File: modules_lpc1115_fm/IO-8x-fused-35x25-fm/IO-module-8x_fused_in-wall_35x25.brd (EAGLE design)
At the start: 35 x 25 mm, 82 parts, among them IC1 LPC1115, IC2 ATAES132A-SHEQ-T, Q2 ASFL, U1 EEPROM, X3 MICROMATCH-10

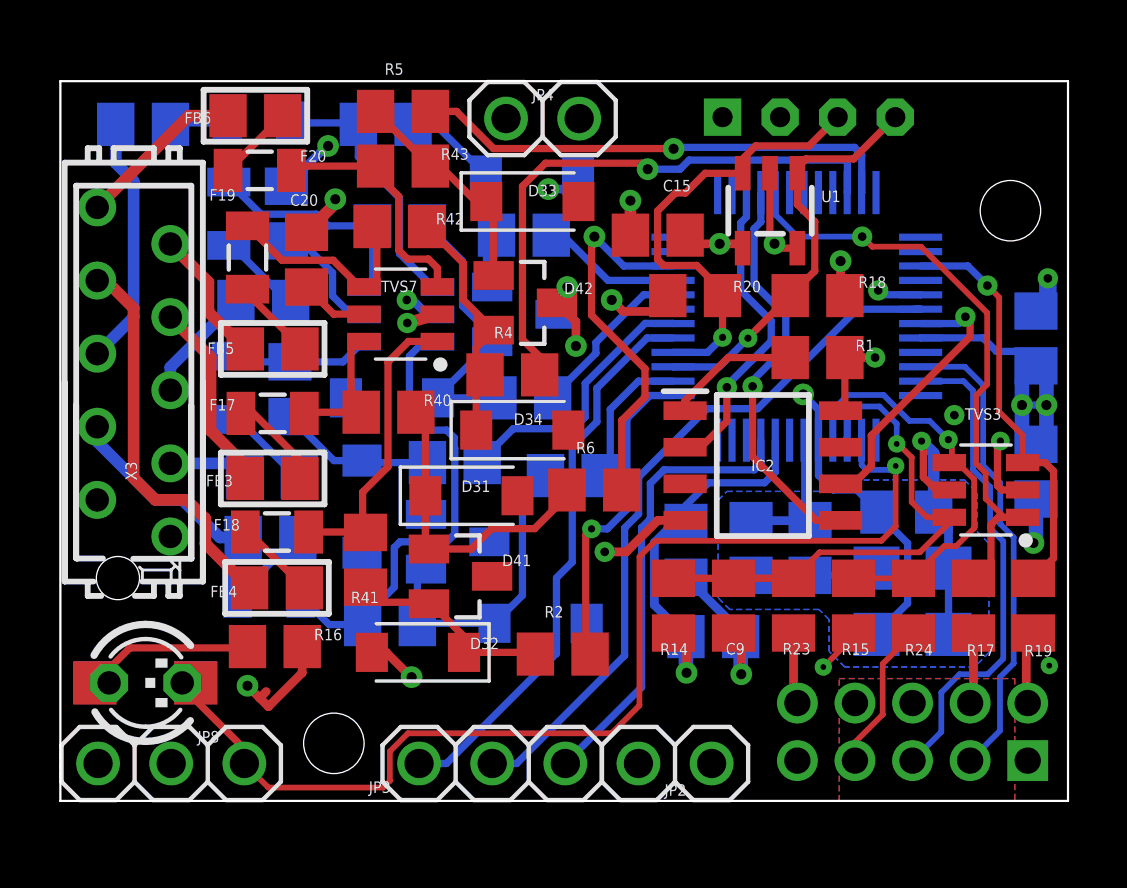
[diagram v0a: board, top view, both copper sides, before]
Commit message: [IOmodule8xUP] added values of 100R resistors; optimized routing
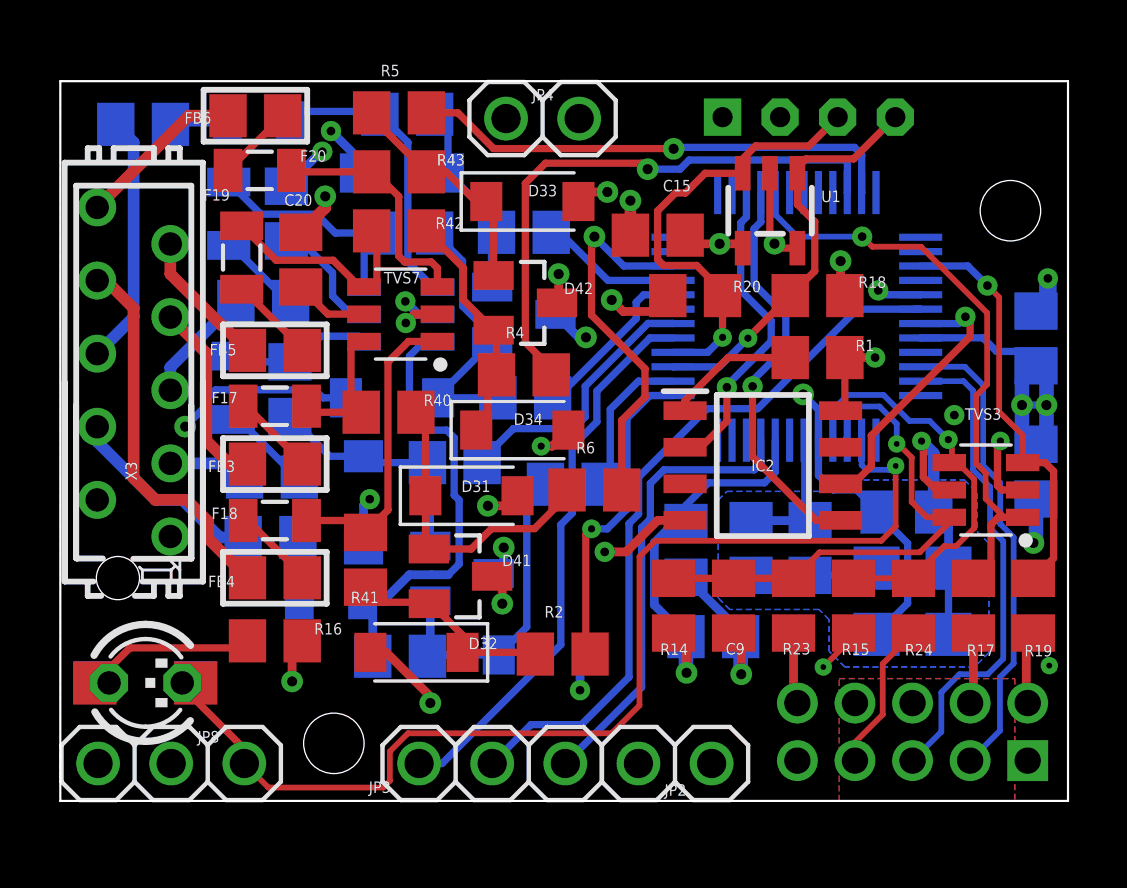
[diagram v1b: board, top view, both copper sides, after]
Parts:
- R2, R3, R4, R5, R6, R7, R8, R9: value 1k -> 100R
- moved D36 4.52 mm to (11.9, 21.8), turned to 0 degrees
- moved F22 2.15 mm to (9.40, 7.06)
- moved R45 1.15 mm to (11.8, 5.03)
- moved D38 1.11 mm to (16.8, 5.07)
- moved D40 1.11 mm to (13.9, 7.90)
- moved R47 0.83 mm to (12.1, 23.9)
- moved FB3 0.51 mm to (7.45, 11.7)
- moved F18 0.41 mm to (7.45, 9.74)
- moved R4 0.40 mm to (16.1, 14.8)
- moved FB4 0.36 mm to (7.45, 7.75)
- moved R46 0.35 mm to (12.1, 19.7)
- moved R3 0.30 mm to (17.8, 11.0)
- moved F17 0.26 mm to (7.45, 13.7)
- moved R43 0.24 mm to (11.8, 21.9)
- moved C20 0.20 mm to (8.35, 18.8)
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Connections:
- net IO1B renamed IO1R
- net IO2B renamed IO2R
- net IO3B renamed IO3R
- net IO4B renamed IO4R
- net IO5B renamed IO5R
- net IO6B renamed IO6R
- net IO7B renamed IO7R
- net IO8B renamed IO8R
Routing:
- net GND: track 40.2 -> 54.9 mm, vias 17 -> 23
- net N$9: track 16.8 -> 15.6 mm
- net IO1R: track 7.26 -> 8.38 mm
- net N$16: track 9.27 -> 10.2 mm
- net N$8: track 3.03 -> 2.11 mm
- net IO7R: track 9.14 -> 8.22 mm
- net +3V3: track 51.6 -> 50.9 mm, vias 12 -> 14
- net N$4: track 3.54 -> 2.97 mm
- net BUS_V: track 25.0 -> 25.5 mm

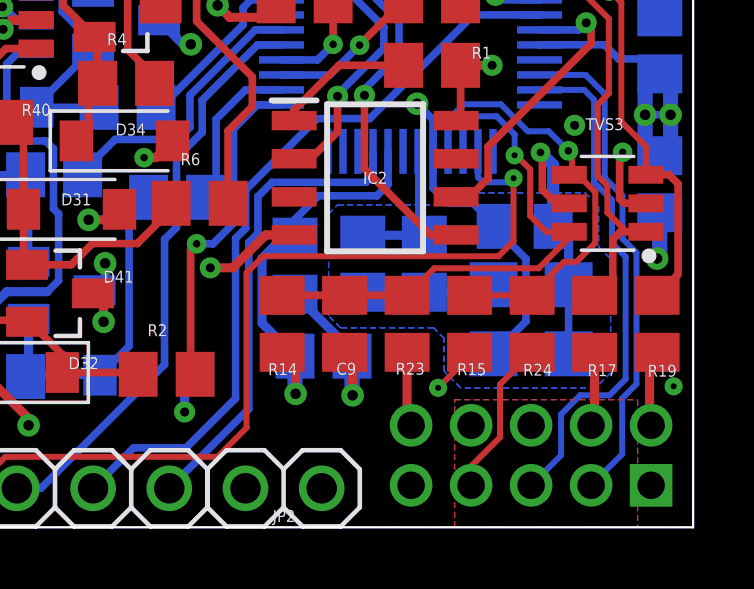
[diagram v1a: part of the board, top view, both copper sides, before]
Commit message: [IOmodule8xUP] moved ISP parts closer to PCB edge
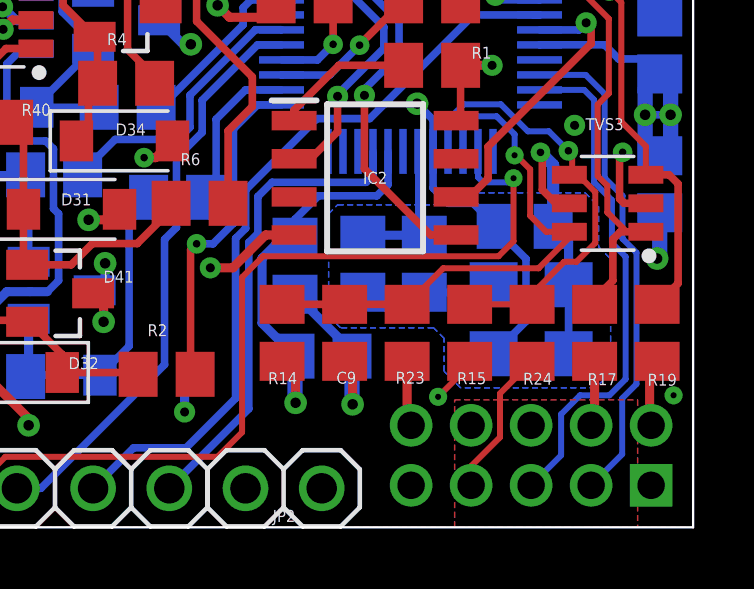
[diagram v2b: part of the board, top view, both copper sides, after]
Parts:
- moved C9 0.30 mm to (23.4, 6.48)
- moved R14 0.30 mm to (21.3, 6.48)
- moved R15 0.30 mm to (27.5, 6.48)
- moved R17 0.30 mm to (31.7, 6.48)
- moved R19 0.30 mm to (33.8, 6.48)
- moved R23 0.30 mm to (25.5, 6.48)
- moved R24 0.30 mm to (29.6, 6.48)

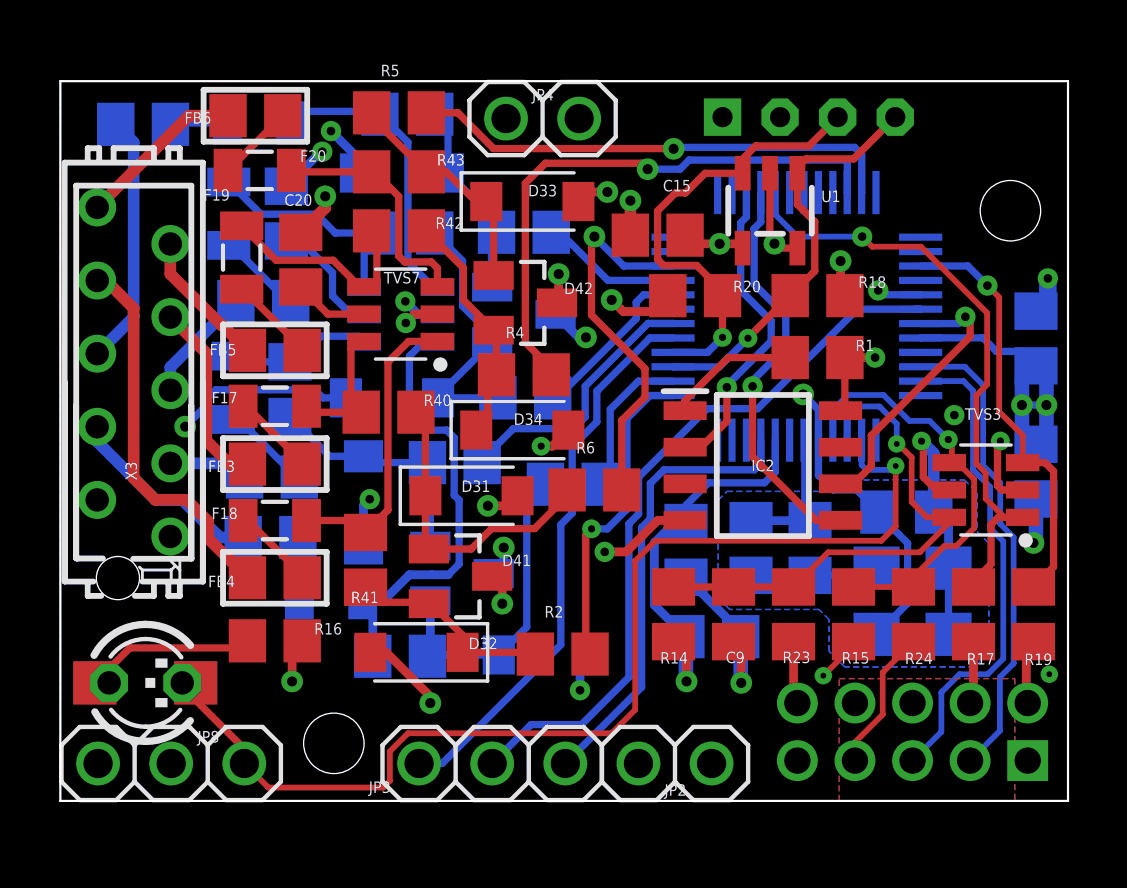
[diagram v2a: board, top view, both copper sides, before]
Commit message: [IOmodule8xUP]  added SPI footprint to SSEL0
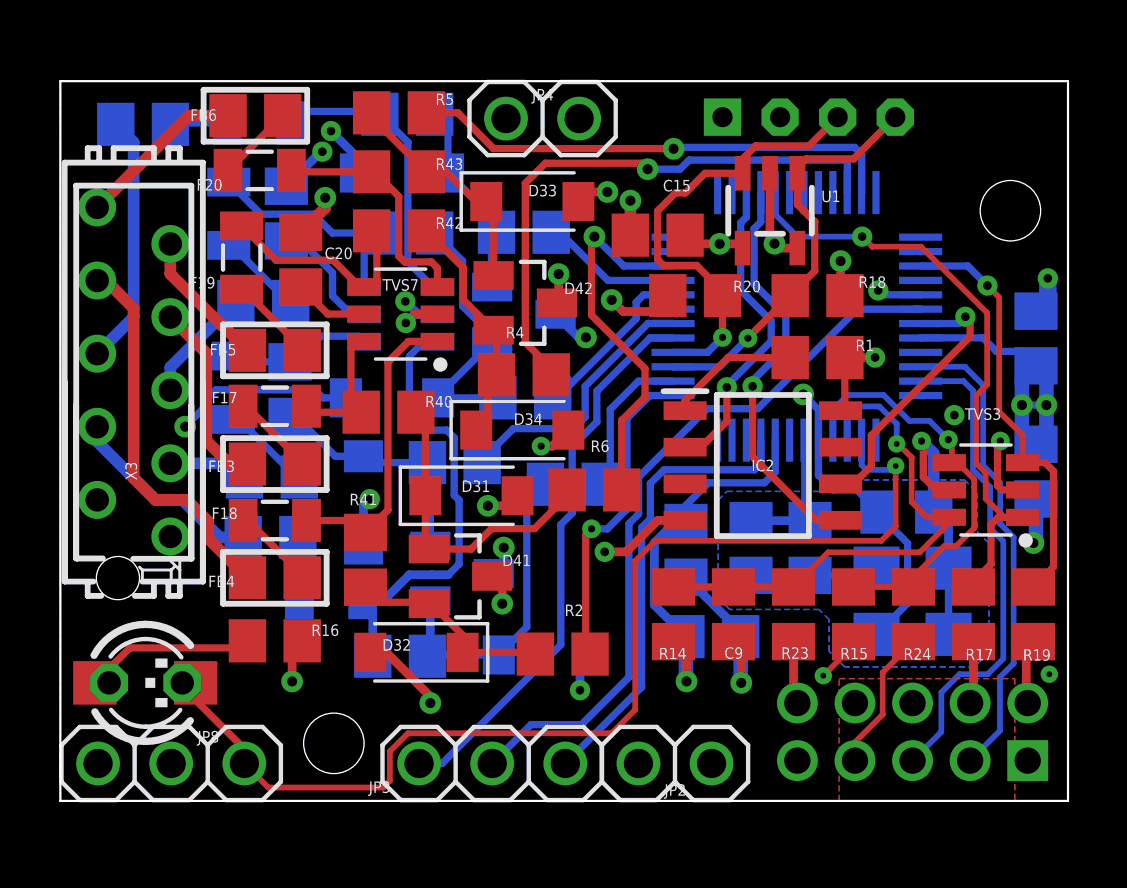
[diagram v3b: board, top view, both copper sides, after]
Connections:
- removed net N$19: IC2.1, R1.1
- new net SSEL0: IC1.10, IC2.1, R1.1
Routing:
- net SSEL0: track 0.00 -> 4.62 mm
- net N$19: track 4.62 -> 0.00 mm

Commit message: [IOmodule8xUP] fixed errors with SPI routing
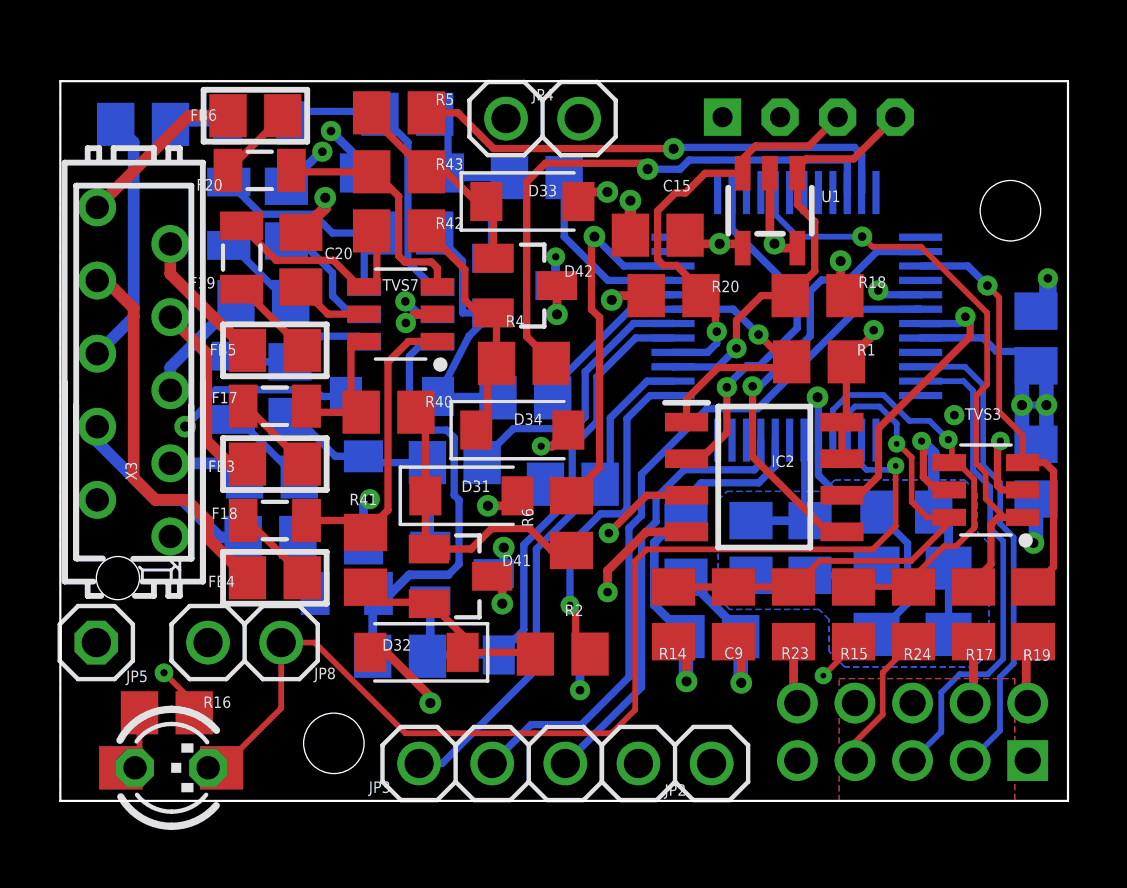
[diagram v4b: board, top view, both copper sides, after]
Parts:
- added JP5: (no value), pinhead_dmx:1X01
- JP8: device pinhead_dmx:1X03 -> pinhead_dmx:1X02
- moved JP8 4.91 mm to (6.40, 5.50)
- moved R16 4.51 mm to (3.70, 3.06)
- moved LED1 3.08 mm to (3.85, 1.15)
- moved LED2 3.08 mm to (3.86, 1.15)
- moved LED3 3.08 mm to (3.85, 1.15)
- moved R8 1.95 mm to (16.6, 21.6)
- moved R6 1.40 mm to (17.8, 9.65), turned to 90 degrees
- moved D39 1.00 mm to (16.1, 17.9)
- moved R20 0.75 mm to (21.3, 17.6)
- moved D42 0.60 mm to (16.1, 17.9)
- moved F22 0.57 mm to (9.95, 7.21)
- moved IC2 0.40 mm to (24.4, 11.2)
- moved R4 0.40 mm to (16.1, 15.2)
- moved R1 0.16 mm to (26.4, 15.2)
- moved D35 0.05 mm to (11.5, 14.1)
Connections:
- removed net MISO0: IC1.27, IC2.2
- removed net MOSI0: IC1.28, IC2.5
- removed net SSEL0: IC1.10, IC2.1, R1.1
- new net MOSI1: IC1.38, IC2.5
- new net SSEL1: IC1.19, IC2.1, R1.1
- net +3V3: now also IC2.3, IC2.7
- net GND: now also JP5.1; no longer JP8.3
- net MISO1: now also IC2.2
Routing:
- net MOSI1: track 0.00 -> 15.3 mm, vias 0 -> 1
- net MOSI0: track 14.2 -> 0.00 mm, vias 1 -> 0
- net MISO1: track 0.00 -> 12.3 mm, vias 0 -> 1
- net MISO0: track 10.9 -> 0.00 mm, vias 1 -> 0
- net SSEL1: track 0.00 -> 9.86 mm, vias 0 -> 1
- net +3V3: track 51.2 -> 55.9 mm, vias 14 -> 15
- net SSEL0: track 4.62 -> 0.00 mm
- net N$41: track 7.10 -> 3.37 mm
- net IO4: track 4.92 -> 6.46 mm
- net IO8R: track 8.02 -> 7.42 mm
- net SDA: track 15.8 -> 15.3 mm
- net IO6: track 11.1 -> 11.7 mm
- net SCL: track 14.3 -> 14.8 mm
- net IO4R: track 6.95 -> 7.48 mm
- net N$9: track 15.6 -> 15.1 mm
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
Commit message: [IOmodule8xUP] several errors fixed - see detailed message
switch to MISO1/MOSI1 with SCK1
changed order of TVS3 and SWD components 
fixed unconnected +3V3 pin at SWD header
fixed width of THT holes for prog button
connected pin 3 and 7 of IC2 to +3V3 so that also a flash IC could beused
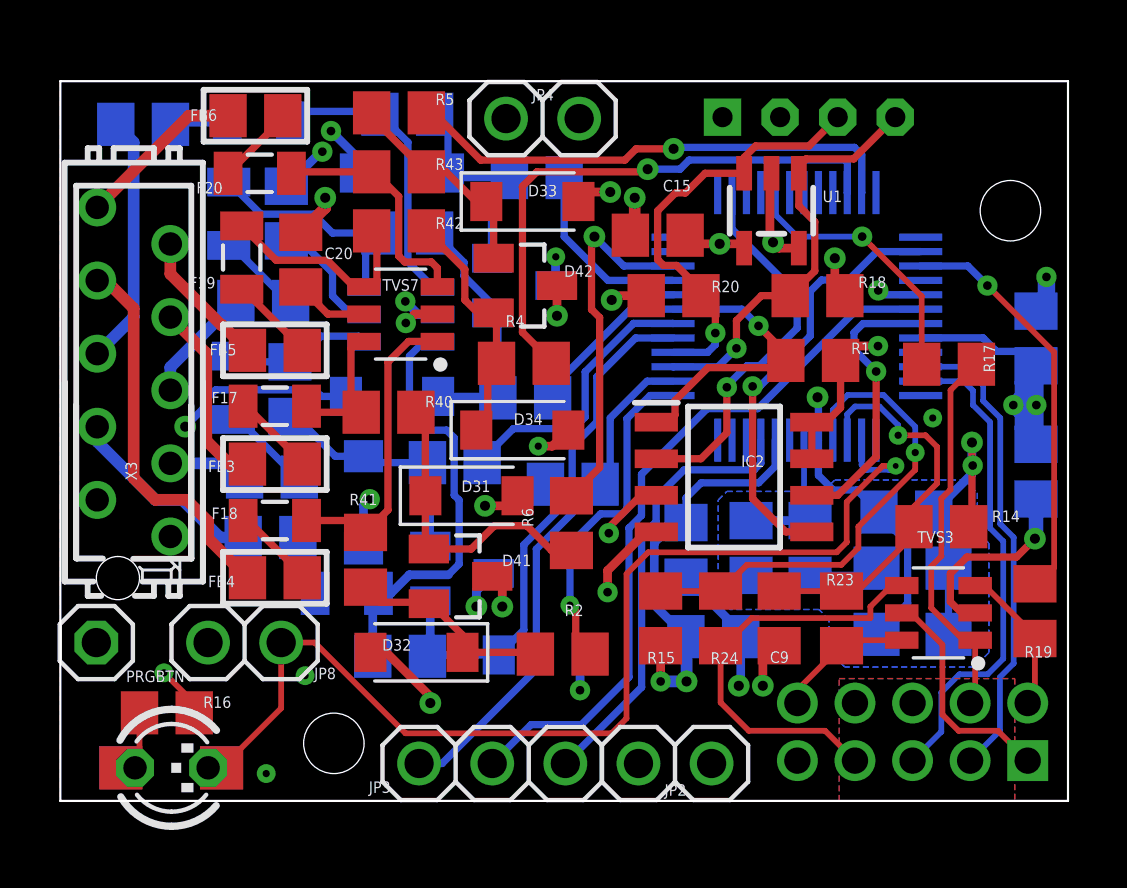
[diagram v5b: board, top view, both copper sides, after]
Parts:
- moved R14 9.79 mm to (30.6, 9.53), turned to 0 degrees
- moved R17 8.73 mm to (30.9, 15.2), turned to 0 degrees
- moved R15 6.70 mm to (20.8, 6.34)
- moved R24 6.70 mm to (22.9, 6.34)
- moved TVS3 4.58 mm to (30.5, 6.53)
- moved R23 1.67 mm to (27.1, 6.34), turned to 90 degrees
- moved C9 1.59 mm to (25.0, 6.34)
- moved IC2 1.05 mm to (23.4, 11.2)
- moved R1 0.21 mm to (26.1, 15.3)
- moved R19 0.12 mm to (33.8, 6.59)
- moved F20 0.10 mm to (6.92, 21.8)
- moved U1 0.05 mm to (24.7, 20.5)
- renumbered JP5 to PRGBTN
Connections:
- net ISP_EN: no longer TVS3.4
- net RESET: now also R23.2; no longer R23.1, TVS3.6
- net SWCLK: no longer TVS3.1
- net SWDIO: no longer TVS3.3
- net SWD_ISP_EN: now also TVS3.4
- net SWD_RESET: now also R23.1, TVS3.6; no longer R23.2
- net SWD_SWCLK: now also JP7.2, R19.2, TVS3.3; no longer JP7.4, R17.2
- net SWD_SWDIO: now also JP7.4, R17.2, TVS3.1; no longer JP7.2, R19.2
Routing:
- net SWCLK: track 21.7 -> 9.39 mm
- net SWD_SWDIO: track 2.26 -> 13.4 mm
- net SWD_ISP_EN: track 4.97 -> 14.9 mm
- net +3V3: track 55.9 -> 63.1 mm, vias 15 -> 16
- net RESET: track 18.5 -> 13.8 mm
- net SWD_RESET: track 2.19 -> 4.80 mm
- net SWD_SWCLK: track 2.63 -> 5.23 mm
- net GND: track 55.6 -> 58.1 mm, vias 22 -> 24
- net ISP_EN: track 15.3 -> 17.1 mm
- net IO3R: track 9.80 -> 8.74 mm
- net MISO1: track 12.3 -> 13.4 mm
- net SSEL1: track 9.86 -> 10.5 mm
- net SWDIO: track 14.8 -> 14.3 mm

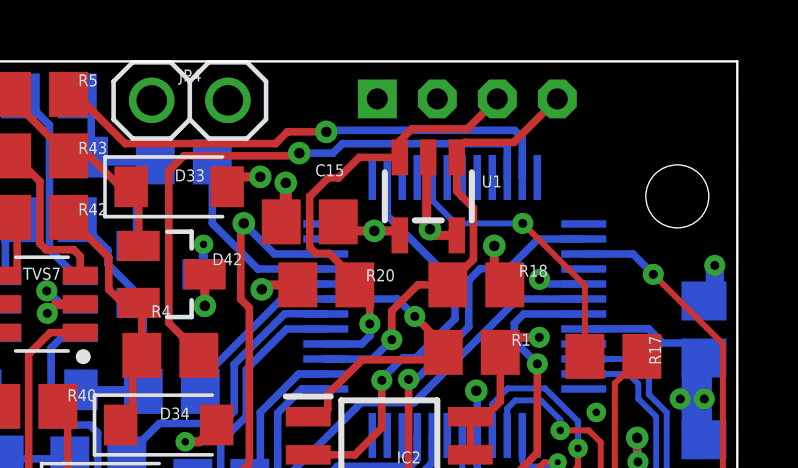
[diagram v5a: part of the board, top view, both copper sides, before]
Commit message: [IOmodule8xUP] added debug RXD / TXD / GND solder pads
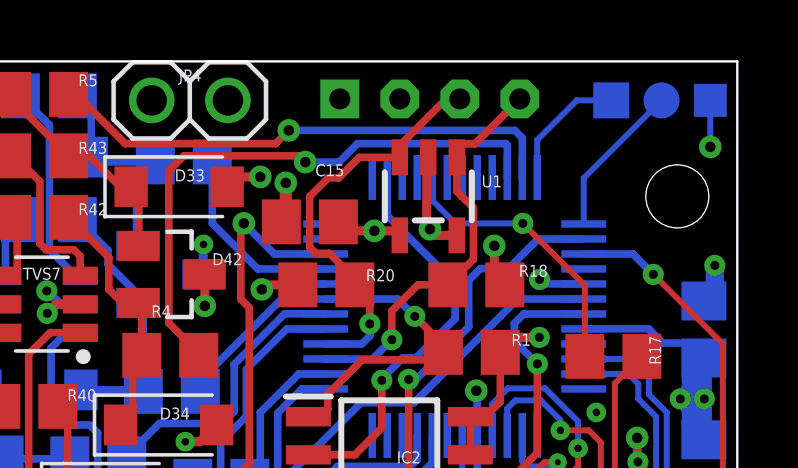
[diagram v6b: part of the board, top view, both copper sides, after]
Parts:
- added GND: TPTP11SQ, testpad:TP11SQ
- added RXD: TPTP12R, testpad:TP12R
- added TXD: TPTP12SQ, testpad:TP12SQ
- moved JP1 1.25 mm to (24.8, 23.8)
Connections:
- new net DBG_RXD: IC1.37, RXD.TP
- new net DBG_TXD: IC1.36, TXD.TP
- net GND: now also GND.TP
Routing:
- net DBG_RXD: track 0.00 -> 5.19 mm
- net DBG_TXD: track 0.00 -> 4.27 mm
- net GND: track 58.1 -> 59.7 mm, vias 24 -> 25
- net SDA: track 15.2 -> 13.9 mm
- net SCL: track 14.8 -> 13.5 mm
